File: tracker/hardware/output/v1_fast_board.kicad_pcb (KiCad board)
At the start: 2 copper layers, 50 x 40 mm, 15 parts, among them U1 ESP32-C3, U2 LR2021F33, U3 MAX-M10S, U4 TPS7A02

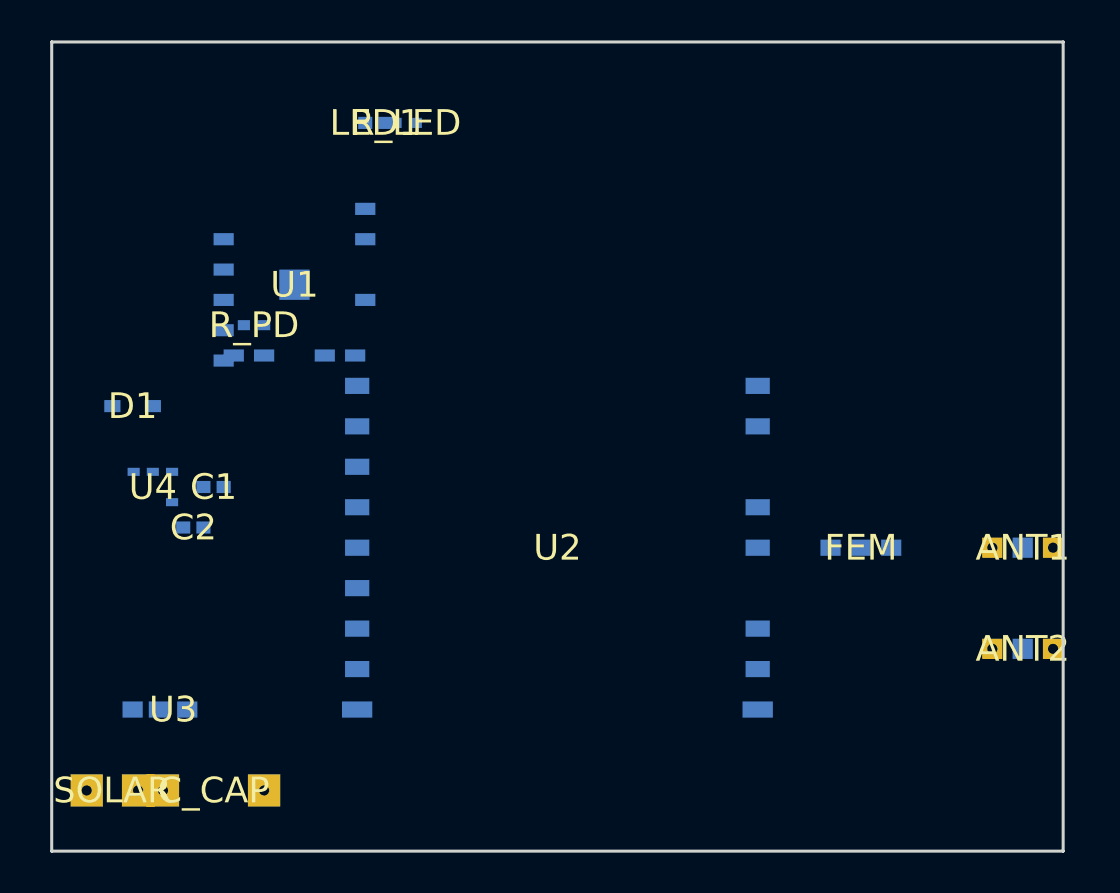
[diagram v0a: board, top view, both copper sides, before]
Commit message: fix(firmware): V1-flight GPIO resolution — drop BMP280/I2C, move LED to GPIO9, gate supercap ADC
- power_manager: compile supercap ADC path behind SUPERCAP_MONITORING; V1
  reports 0 mV (ADC1_CH0=GPIO0=GPS TX, no free ADC pin).
- app_main: LED_GPIO 18->9 (GPIO9 was I2C SDA); i2c_scan compiled out when
  BMP280 disabled.
- radio_test: LED_PIN 8->9 for PCB V1.
- Kconfig: BMP280 default n; FEM_TX_PIN default -1 (GPIO19 absent on C3 Mini V1).
- tests: pin expectation updates.
- DISCOVERIES: append balloon-hermes discovery sync entries.
- v1_fast_board.kicad_pcb: routed board update.

Preserved from pcbprog/base-d14-freeze working tree during the credential-literal
history scrub; committed on a clean rewritten base.
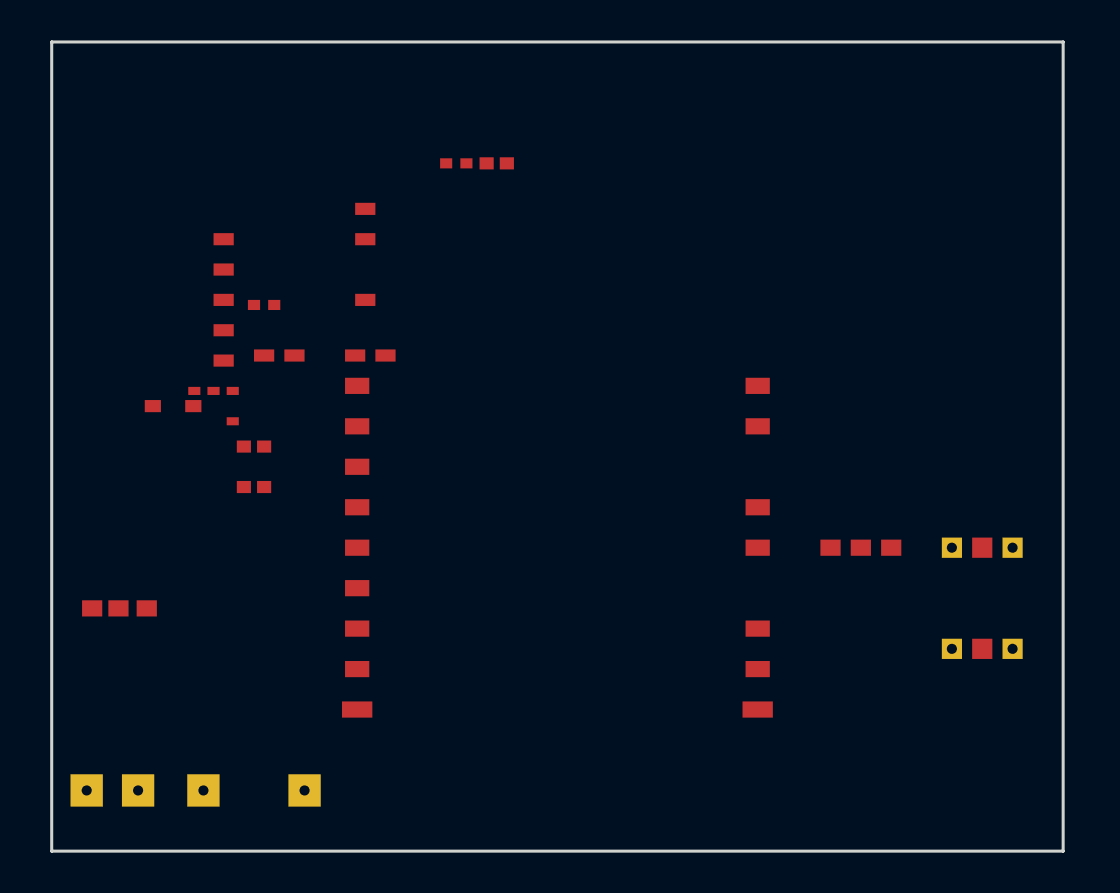
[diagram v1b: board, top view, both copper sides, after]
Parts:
- moved LED1 6.32 mm to (22.0, 6.00)
- moved U3 5.39 mm to (4.00, 28.0)
- moved U4 5.00 mm to (8.00, 18.0)
- moved C2 3.61 mm to (10.0, 22.0)
- moved R_LED 3.20 mm to (20.0, 6.00)
- moved C1 2.83 mm to (10.0, 20.0)
- moved ANT1 2.00 mm to (46.0, 25.0)
- moved ANT2 2.00 mm to (46.0, 30.0)
- moved C_CAP 2.00 mm to (10.0, 37.0)
- moved D1 2.00 mm to (6.00, 18.0)
- moved R_PD 1.12 mm to (10.5, 13.0)
